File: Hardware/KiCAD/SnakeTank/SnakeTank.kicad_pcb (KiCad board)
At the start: 4 copper layers, 80.5 x 36.6 mm, 51 parts, among them J1 Conn_01x12, J2 USB_C_Receptacle_USB2.0_16P, J3 RJ45, Q1 L8050QLT1G, Q2 L8050QLT1G, U1 LP2985-3.3, U2 ESP32-S3-WROOM-1-N8, U4 FT231XS

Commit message: WOOOHOO
rough draft of layout done
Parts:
- added G***: LOGO, graphics:snakeLogo, F.Cu at (95.9, 35.9)
- TP4, TP5: footprint TestPoint:TestPoint_Plated_Hole_D2.0mm -> TestPoint:TestPoint_Keystone_5019_Minature
- moved DS1 42.5 mm to (26.4, 58.0)
- moved TP3 39.4 mm to (64.1, 47.6)
- moved TP2 15.2 mm to (59.6, 44.1)
- moved TP5 10.5 mm to (73.3, 58.4)
- moved R12 6.05 mm to (67.8, 40.4)
- moved R13 5.85 mm to (67.8, 38.1)
- moved R14 5.66 mm to (67.8, 35.8)
- moved R15 5.47 mm to (67.8, 33.5)
- moved R3 4.13 mm to (62.5, 27.9), turned to -90 degrees
- moved C12 3.89 mm to (62.5, 31.2), turned to -90 degrees
- moved C4 2.17 mm to (60.7, 31.2), turned to -90 degrees
- moved TP4 1.84 mm to (44.2, 30.4)
- moved R1 1.40 mm to (23.5, 27.2)
- moved C7 1.02 mm to (38.1, 41.4), turned to -90 degrees
- moved C14 0.80 mm to (34.8, 42.2), turned to 0 degrees
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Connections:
- U2 pad 41_10: (no net) -> GND
- U2 pad 41_11: (no net) -> GND
- U2 pad 41_12: (no net) -> GND
- U2 pad 41_13: (no net) -> GND
- U2 pad 41_14: (no net) -> GND
- U2 pad 41_15: (no net) -> GND
- U2 pad 41_16: (no net) -> GND
- U2 pad 41_17: (no net) -> GND
- U2 pad 41_18: (no net) -> GND
- U2 pad 41_19: (no net) -> GND
- U2 pad 41_20: (no net) -> GND
- U2 pad 41_21: (no net) -> GND
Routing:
- net GND: track 4.21 -> 56.2 mm, vias 0 -> 51
- net +5V: track 0.00 -> 47.7 mm
- net +3.3V: track 0.00 -> 31.5 mm
- net ESP_3V3: track 3.60 -> 14.0 mm, vias 0 -> 2
- net Net-(FB1-Pad2): track 2.62 -> 9.85 mm, vias 0 -> 2
- net /GPIO_0: track 70.6 -> 75.7 mm
- net /USBN: track 0.00 -> 4.54 mm
- net /USBP: track 0.00 -> 4.12 mm
- net Net-(J2-CC1): track 8.70 -> 5.72 mm
- net LCD_D4: track 33.2 -> 36.0 mm
- net /CHIP_PU: track 36.4 -> 33.7 mm, vias 0 -> 2
- net LCD_E: track 46.0 -> 48.2 mm
- net Net-(U4-3V3OUT): track 13.5 -> 11.3 mm
- net LCD_RS: track 51.9 -> 53.2 mm
- net DHT11_4_data: track 50.9 -> 52.2 mm, vias 0 -> 1
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- added copper zone on B.Cu, net GND
- added copper zone on F.Cu, net GND
- added copper zone on In1.Cu, net GND
- added copper zone on In2.Cu, net GND
- removed copper zone on B.Cu, net +5V
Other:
- board size 80.5 x 36.6 mm -> 80.8 x 37.1 mm
- board text added: "For Kynes :) -VIP"
- board text added: "GPIO"
- board text added: "Sensors"
- board text added: "SnakeTank Rev1.0 241027"

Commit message: Hw tweaks
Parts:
- moved G*** 23.4 mm to (86.6, 57.4)
- moved C1 3.78 mm to (54.1, 40.1), turned to 0 degrees
- moved R11 0.76 mm to (49.5, 37.8)
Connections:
- U2 pad 41_10: GND -> (no net)
- U2 pad 41_11: GND -> (no net)
- U2 pad 41_12: GND -> (no net)
- U2 pad 41_13: GND -> (no net)
- U2 pad 41_14: GND -> (no net)
- U2 pad 41_15: GND -> (no net)
- U2 pad 41_16: GND -> (no net)
- U2 pad 41_17: GND -> (no net)
- U2 pad 41_18: GND -> (no net)
- U2 pad 41_19: GND -> (no net)
- U2 pad 41_20: GND -> (no net)
- U2 pad 41_21: GND -> (no net)
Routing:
- net +5V: track 47.7 -> 128.7 mm
- net GND: track 56.2 -> 46.3 mm, vias 51 -> 152
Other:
- board text removed: "For Kynes :) -VIP"

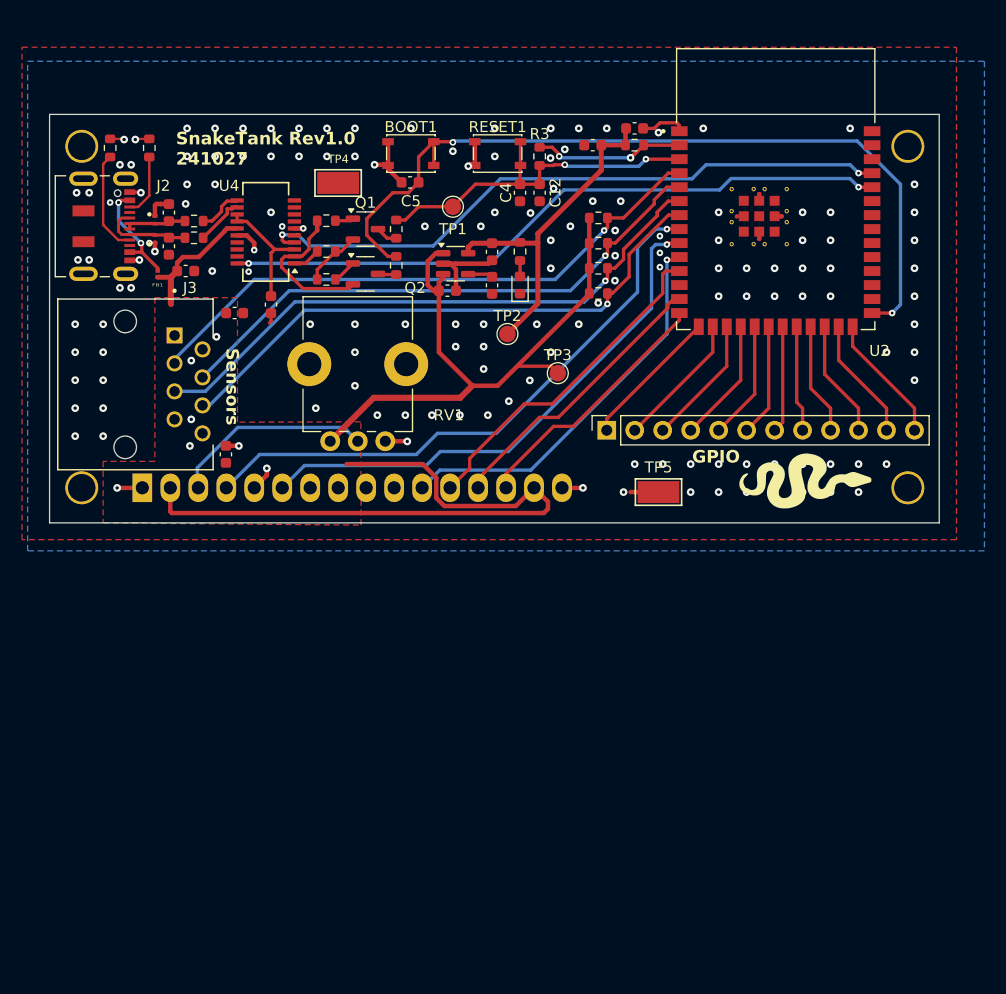
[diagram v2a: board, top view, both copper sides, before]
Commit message: PCB ordered rev 1
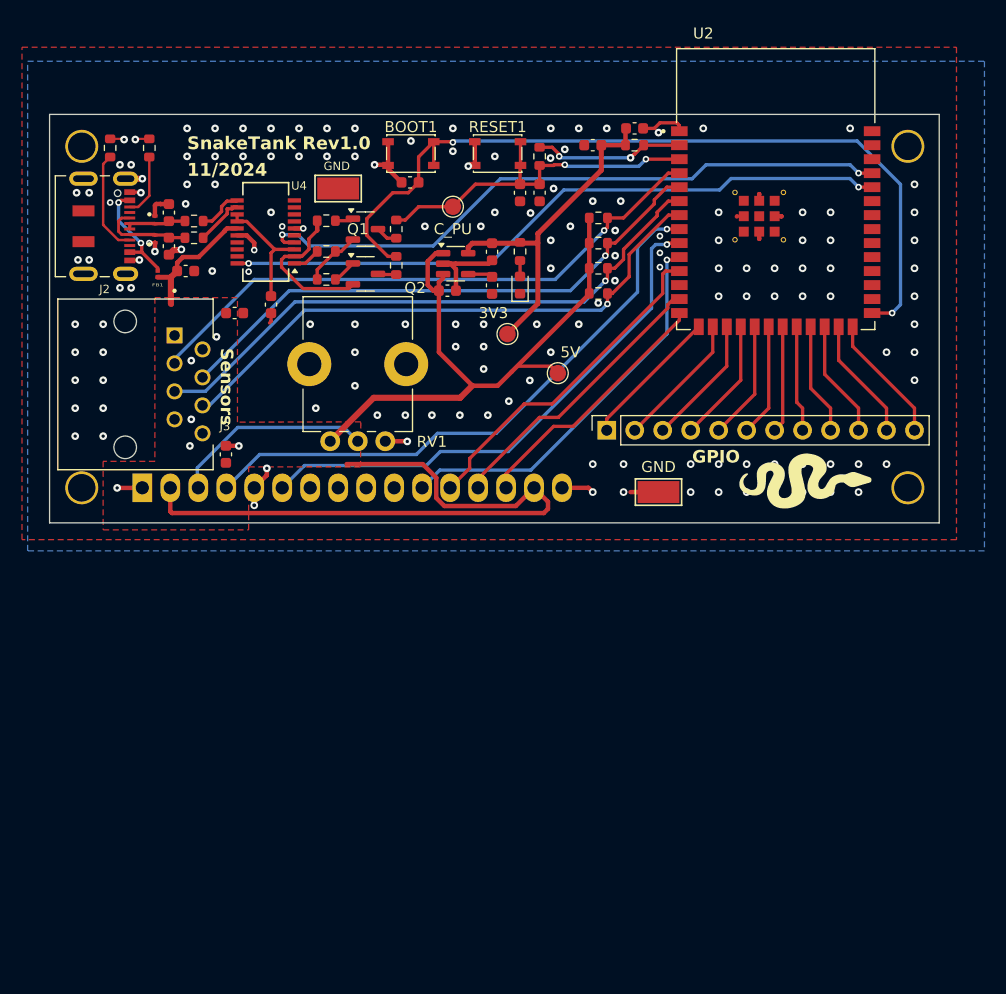
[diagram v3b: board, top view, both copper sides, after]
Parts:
- moved GND 0.51 mm to (44.2, 30.9)
- renumbered TP2 to 3V3, TP3 to 5V, TP1 to C_PU, TP4 to GND, TP5 to GND
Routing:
- net GND: track 46.3 -> 51.8 mm, vias 152 -> 155
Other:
- board text added: "11/2024"
- board text added: "SnakeTank Rev1.0"
- board text removed: "SnakeTank Rev1.0 241027"
